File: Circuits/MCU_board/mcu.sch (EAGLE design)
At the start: 54 parts, among them IC1 RP111N331B-TR-FE, U1 TCA9548APWR, U2 USBLC6-2P6, U4 LSM9DS1, U5 STM32L452RECT6

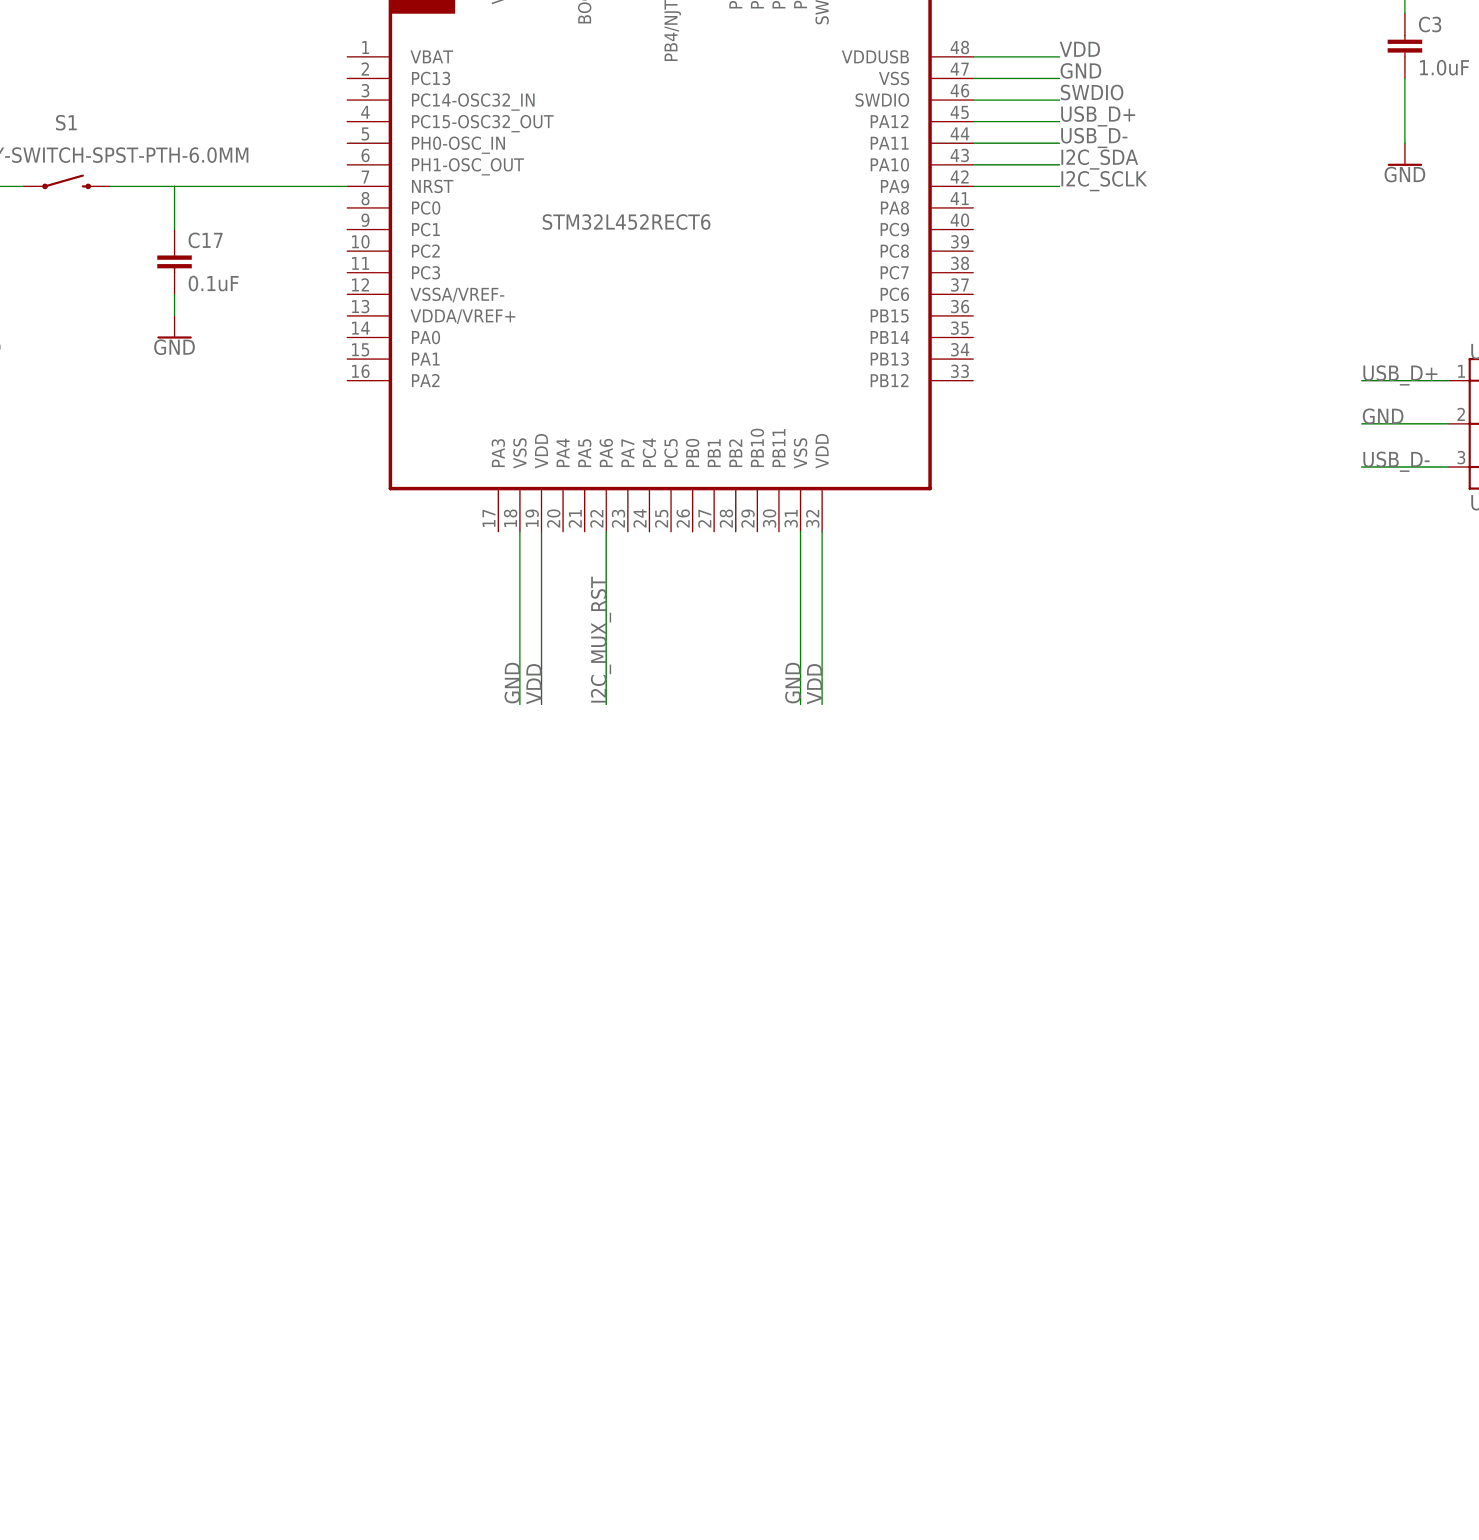
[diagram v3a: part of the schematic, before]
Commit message: Add FTDI chip to MCU board
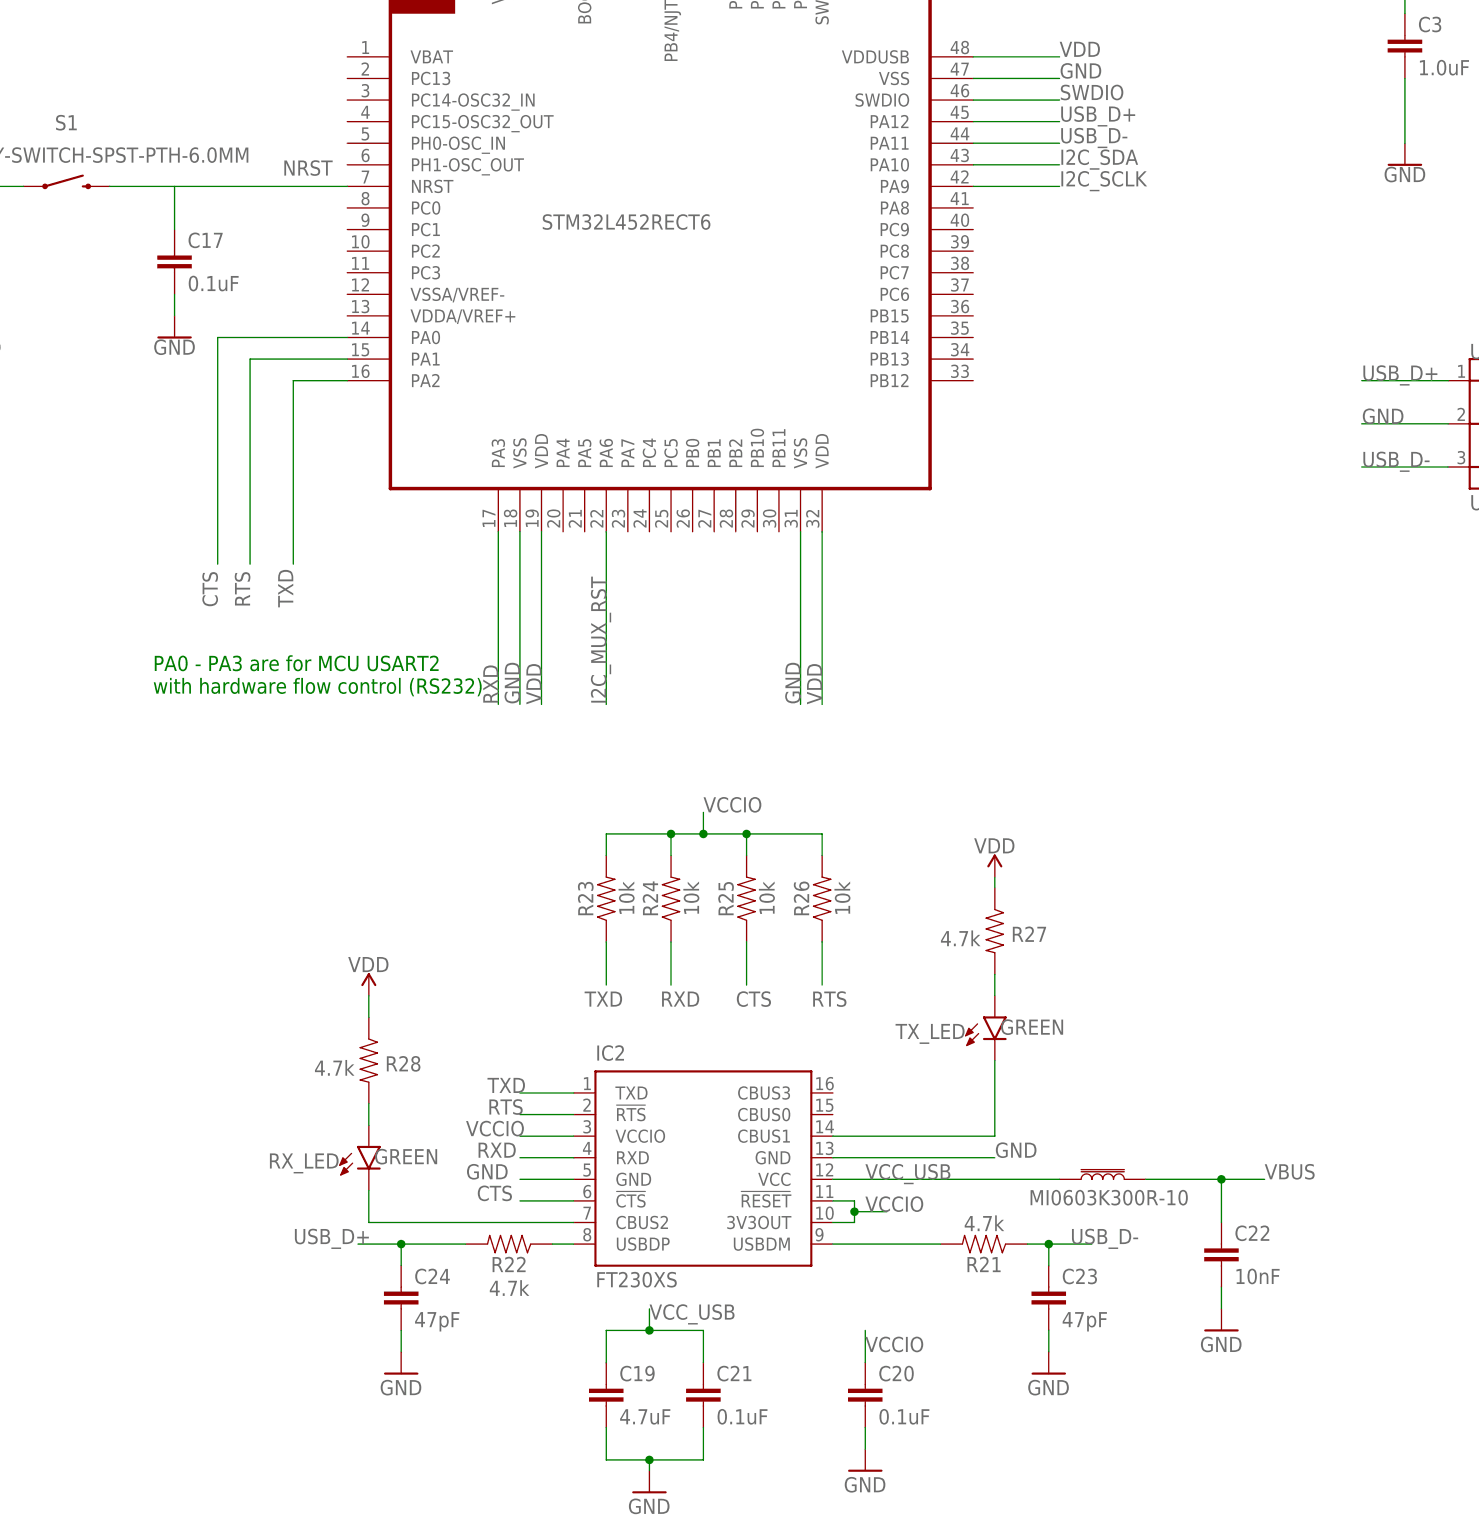
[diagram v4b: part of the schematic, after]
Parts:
- added C19: 4.7uF, SparkFun-Capacitors:4.7UF-0603-6.3V-(10%)
- added C20, C21: 0.1uF, SparkFun-Capacitors:0.1UF-0603-25V-(+80/-20%)
- added C22: 10nF, SparkFun-Capacitors:10NF-0603-50V-10%
- added C23, C24: 47pF, SparkFun-Capacitors:47PF-0603-50V-5%
- added IC2: FT230XS, ftdichip:FT230XS
- added MI0603K300R-10: 30Ω/1.8A, SparkFun-Coils:FERRITE_BEAD-0603
- added R21, R22, R27, R28: 4.7k, SparkFun-Resistors:4.7KOHM-0603-1/10W-1%
- added R23, R24, R25, R26: 10k, SparkFun-Resistors:10KOHM-0603-1/10W-1%
- added RX_LED, TX_LED: GREEN, SparkFun-LED:LED-GREEN0603
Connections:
- net N$4 renamed NRST
- new net CTS: IC2.!CTS, R25.1, U5.PA0
- new net N$10: R28.2, RX_LED.A
- new net N$11: IC2.CBUS2, RX_LED.C
- new net N$6: IC2.USBDM, R21.2
- new net N$7: IC2.USBDP, R22.1
- new net N$8: R27.2, TX_LED.A
- new net N$9: IC2.CBUS1, TX_LED.C
- new net RTS: IC2.!RTS, R26.1, U5.PA1
- new net RXD: IC2.RXD, R24.1, U5.PA3
- new net TXD: IC2.TXD, R23.1, U5.PA2
- new net VCCIO: C20.1, IC2.!RESET, IC2.3V3OUT, IC2.VCCIO, R23.2, R24.2, R25.2, R26.2
- new net VCC_USB: C19.1, C21.1, IC2.VCC, MI0603K300R-10.1
- net GND: now also C19.2, C20.2, C21.2, C22.2, C23.2, C24.2, IC2.GND, IC2.GND@1
- net USB_D+: now also C24.1, R22.2
- net USB_D-: now also C23.1, R21.1
- net VBUS: now also C22.1, MI0603K300R-10.2
- net VDD: now also R27.1, R28.1
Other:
- note added: "PA0 - PA3 are for MCU USART2 with hardware flow control (RS232)"

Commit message: Fix resistors in FTDI
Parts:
- R21, R22: value 4.7k -> 27R
- R27, R28: value 4.7k -> 270R
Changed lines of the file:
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@@
 <part name="IC2" library="ftdichip" library_urn="urn:adsk.eagle:library:231" deviceset="FT230X" device="S" package3d_urn="urn:adsk.eagle:package:14016/1"/>
 <part name="MI0603K300R-10" library="SparkFun-Coils" deviceset="FERRITE_BEAD" device="-0603" value="30Ω/1.8A"/>
-<part name="R21" library="SparkFun-Resistors" deviceset="4.7KOHM" device="-0603-1/10W-1%" value="4.7k"/>
-<part name="R22" library="SparkFun-Resistors" deviceset="4.7KOHM" device="-0603-1/10W-1%" value="4.7k"/>
+<part name="R21" library="SparkFun-Resistors" deviceset="4.7KOHM" device="-0603-1/10W-1%" value="27R"/>
+<part name="R22" library="SparkFun-Resistors" deviceset="4.7KOHM" device="-0603-1/10W-1%" value="27R"/>
 <part name="C19" library="SparkFun-Capacitors" deviceset="4.7UF" device="-0603-6.3V-(10%)" value="4.7uF"/>
 <part name="C20" library="SparkFun-Capacitors" deviceset="0.1UF" device="-0603-25V-(+80/-20%)" value="0.1uF"/>
@@
 <part name="C23" library="SparkFun-Capacitors" deviceset="47PF" device="-0603-50V-5%" value="47pF"/>
 <part name="C24" library="SparkFun-Capacitors" deviceset="47PF" device="-0603-50V-5%" value="47pF"/>
-<part name="R27" library="SparkFun-Resistors" deviceset="4.7KOHM" device="-0603-1/10W-1%" value="4.7k"/>
+<part name="R27" library="SparkFun-Resistors" deviceset="4.7KOHM" device="-0603-1/10W-1%" value="270R"/>
 <part name="TX_LED" library="SparkFun-LED" deviceset="LED-GREEN" device="0603" value="GREEN"/>
 <part name="GND26" library="supply1" library_urn="urn:adsk.eagle:library:371" deviceset="GND" device=""/>
@@
 <part name="SUPPLY24" library="SparkFun-PowerSymbols" deviceset="VDD" device=""/>
 <part name="RX_LED" library="SparkFun-LED" deviceset="LED-GREEN" device="0603" value="GREEN"/>
-<part name="R28" library="SparkFun-Resistors" deviceset="4.7KOHM" device="-0603-1/10W-1%" value="4.7k"/>
+<part name="R28" library="SparkFun-Resistors" deviceset="4.7KOHM" device="-0603-1/10W-1%" value="270R"/>
 <part name="SUPPLY25" library="SparkFun-PowerSymbols" deviceset="VDD" device=""/>
 <part name="GND29" library="supply1" library_urn="urn:adsk.eagle:library:371" deviceset="GND" device=""/>

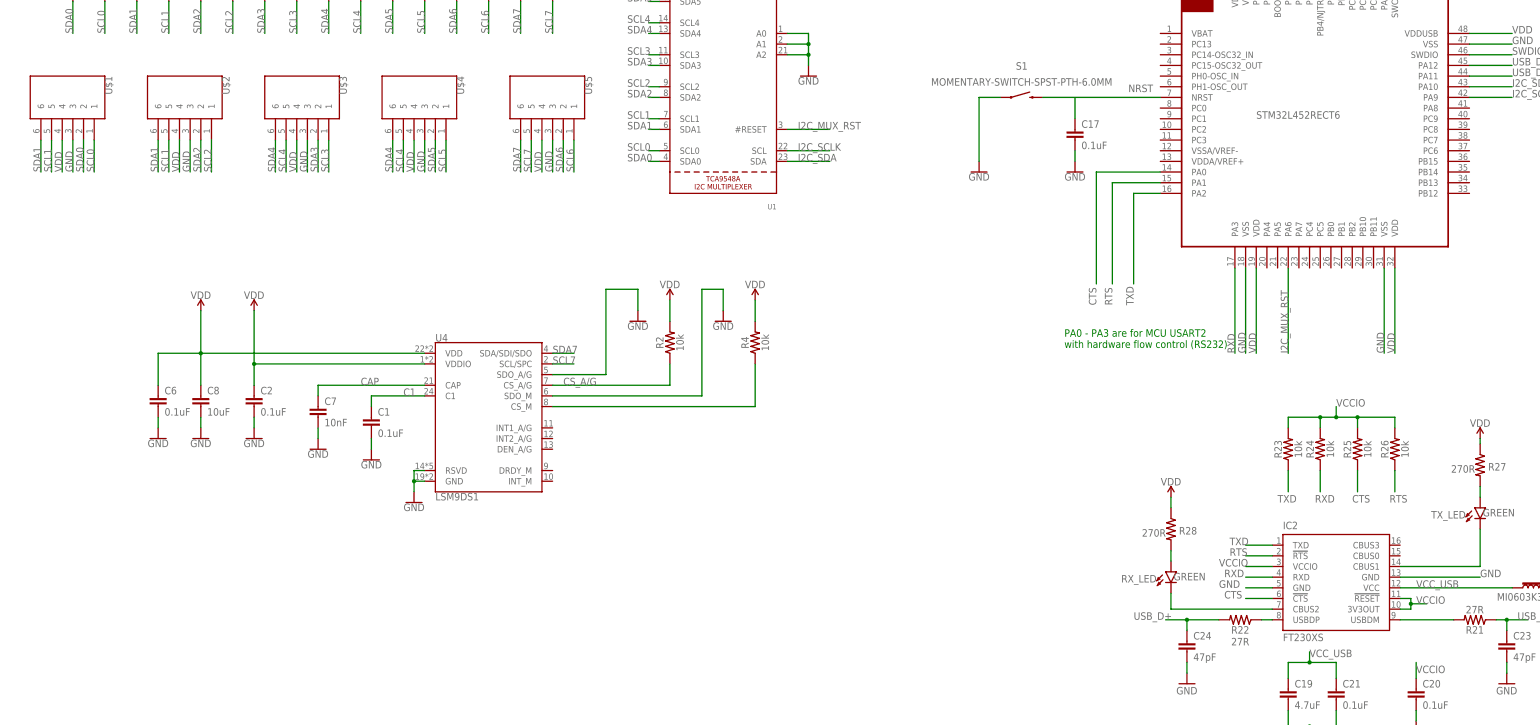
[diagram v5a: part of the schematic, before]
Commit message: Fixed connector mistakes, preliminary placement of all components
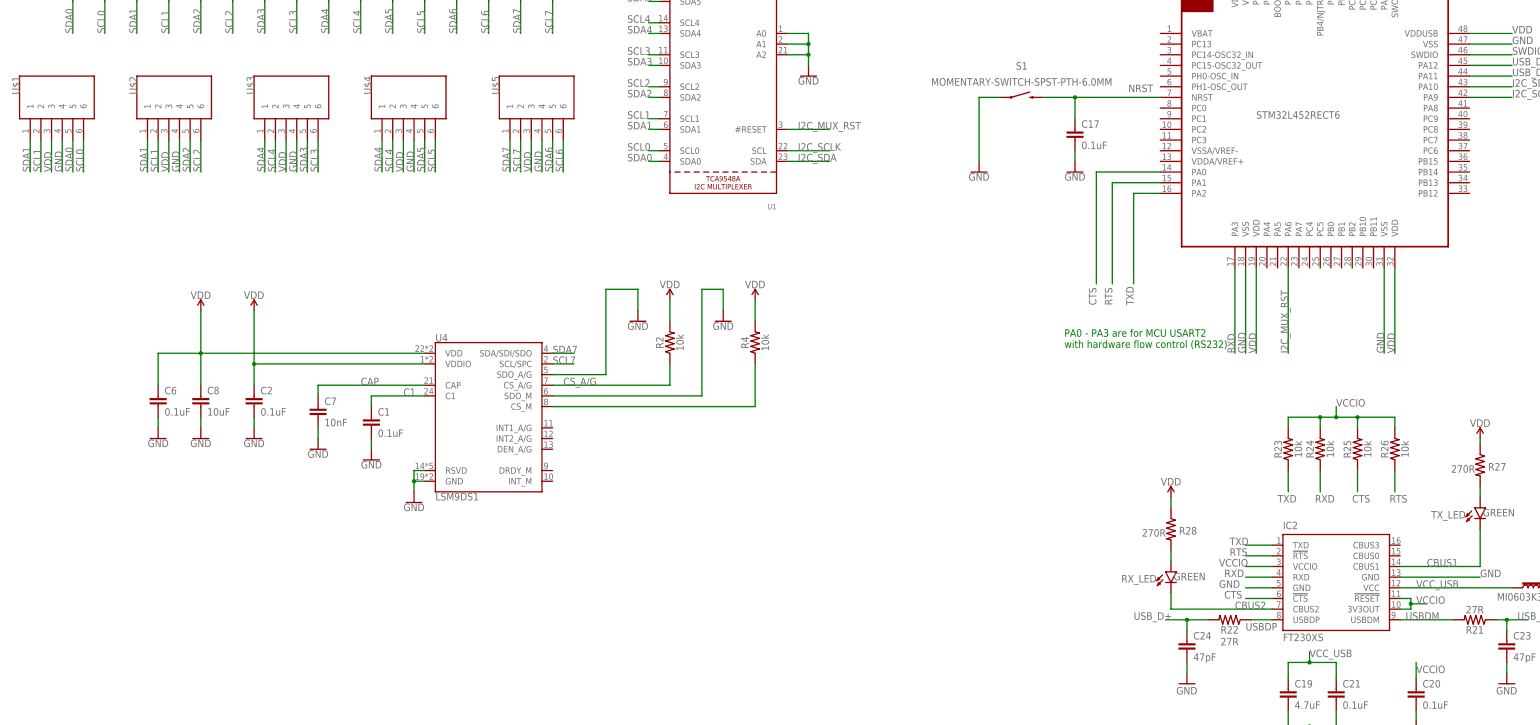
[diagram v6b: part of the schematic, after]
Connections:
- net N$11 renamed CBUS2
- net N$6 renamed USBDM
- net N$7 renamed USBDP
- net N$9 renamed CBUS1
- removed net N$3: C17.1
- net GND: now also U$1.4, U$2.4, U$3.4, U$4.4, U$5.4; no longer U$1.3, U$2.3, U$3.3, U$4.3, U$5.3
- net NRST: now also C17.1
- net SCL0: now also U$1.6; no longer U$1.1
- net SCL1: now also U$1.2, U$2.2; no longer U$1.5, U$2.5
- net SCL2: now also U$2.6; no longer U$2.1
- net SCL3: now also U$3.6; no longer U$3.1
- net SCL4: now also U$3.2, U$4.2; no longer U$3.5, U$4.5
- net SCL5: now also U$4.6; no longer U$4.1
- net SCL6: now also U$5.6; no longer U$5.1
- net SCL7: now also U$5.2; no longer U$5.5
- net SDA0: now also U$1.5; no longer U$1.2
- net SDA1: now also U$1.1, U$2.1; no longer U$1.6, U$2.6
- net SDA2: now also U$2.5; no longer U$2.2
- net SDA3: now also U$3.5; no longer U$3.2
- net SDA4: now also U$3.1, U$4.1; no longer U$3.6, U$4.6
- net SDA5: now also U$4.5; no longer U$4.2
- net SDA6: now also U$5.5; no longer U$5.2
- net SDA7: now also U$5.1; no longer U$5.6
- net VDD: now also U$1.3, U$2.3, U$3.3, U$4.3, U$5.3; no longer U$1.4, U$2.4, U$3.4, U$4.4, U$5.4
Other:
- moved on the sheet: R22, U$1, U$2, U$3, U$4, U$5

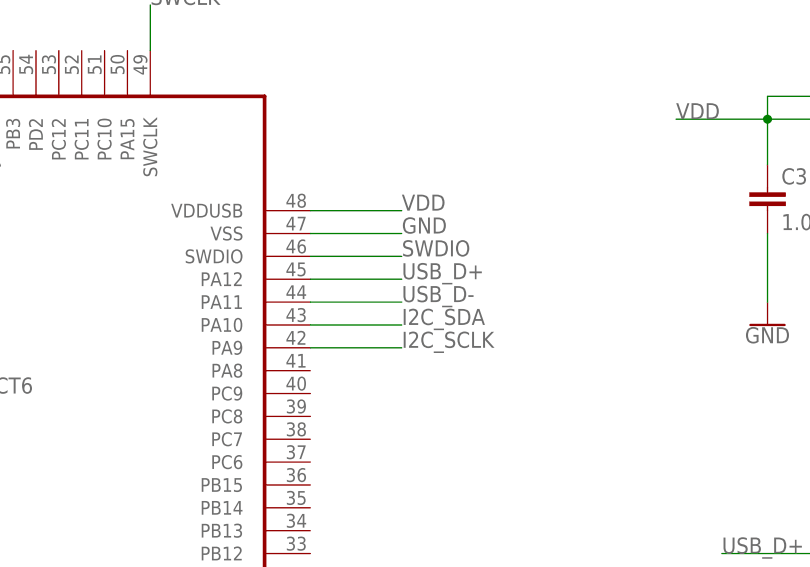
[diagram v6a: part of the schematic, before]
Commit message: Changed location of components
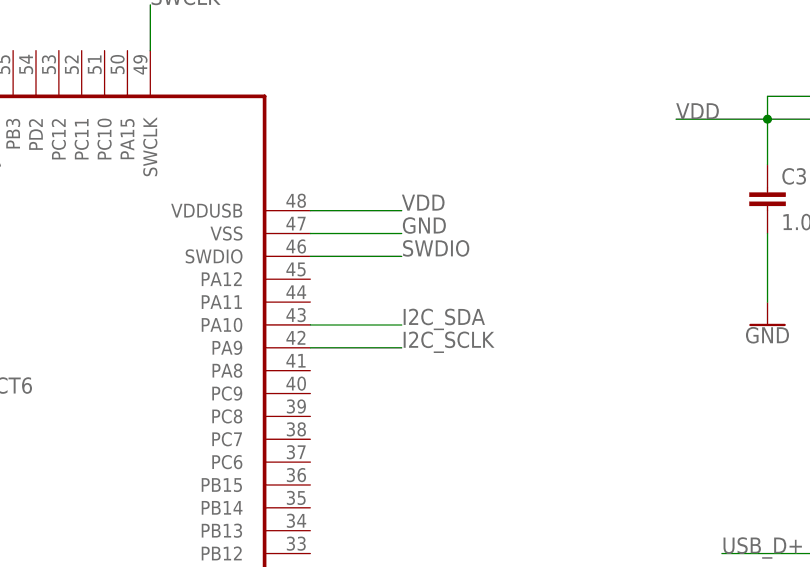
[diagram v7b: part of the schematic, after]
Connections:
- net USB_D+: no longer U5.PA12
- net USB_D-: no longer U5.PA11
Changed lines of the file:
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@@
 <net name="USB_D-" class="0">
-<segment>
-<pinref part="U5" gate="G$1" pin="PA11"/>
-<wire x1="124.46" y1="96.52" x2="134.62" y2="96.52" width="0.1524" layer="91"/>
-<label x="134.62" y="96.52" size="1.778" layer="95"/>
-</segment>
 <segment>
 <pinref part="U2" gate="G$1" pin="I/O2_1"/>
@@
 <net name="USB_D+" class="0">
 <segment>
-<pinref part="U5" gate="G$1" pin="PA12"/>
-<wire x1="124.46" y1="99.06" x2="134.62" y2="99.06" width="0.1524" layer="91"/>
-<label x="134.62" y="99.06" size="1.778" layer="95"/>
-</segment>
-<segment>
 <pinref part="U2" gate="G$1" pin="I/O1_1"/>
